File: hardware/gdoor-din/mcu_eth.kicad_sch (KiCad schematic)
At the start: 60 parts, among them J101 USB-C, J102 HR911105A, J103 EXP, SW101 RESET, SW102 BOOT, U101 ESP32-S3-WROOM-1-N8R2, U102 USBLC6-2SC6, U103 AMS1117-3.3, U104 W5500, Y101 25MHz

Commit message: gdoor-din: give SW101/SW102 one value so JLC merges their BOM line
Both buttons are the same part (C318884); the values RESET and BOOT
made two BOM lines matched to one part, which JLC flags. Both are now
"TL3342"; the schematic net labels still say which is which.

Co-Authored-By: Claude Opus 5.5 <noreply@anthropic.com>
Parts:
- SW101: value RESET -> TL3342
- SW102: value BOOT -> TL3342
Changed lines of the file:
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@@
 			)
 		)
-		(property "Value" "RESET"
+		(property "Value" "TL3342"
 			(at 99.06 80.01 0)
 			(show_name no)
@@
 			)
 		)
-		(property "Value" "BOOT"
+		(property "Value" "TL3342"
 			(at 99.06 92.71 0)
 			(show_name no)

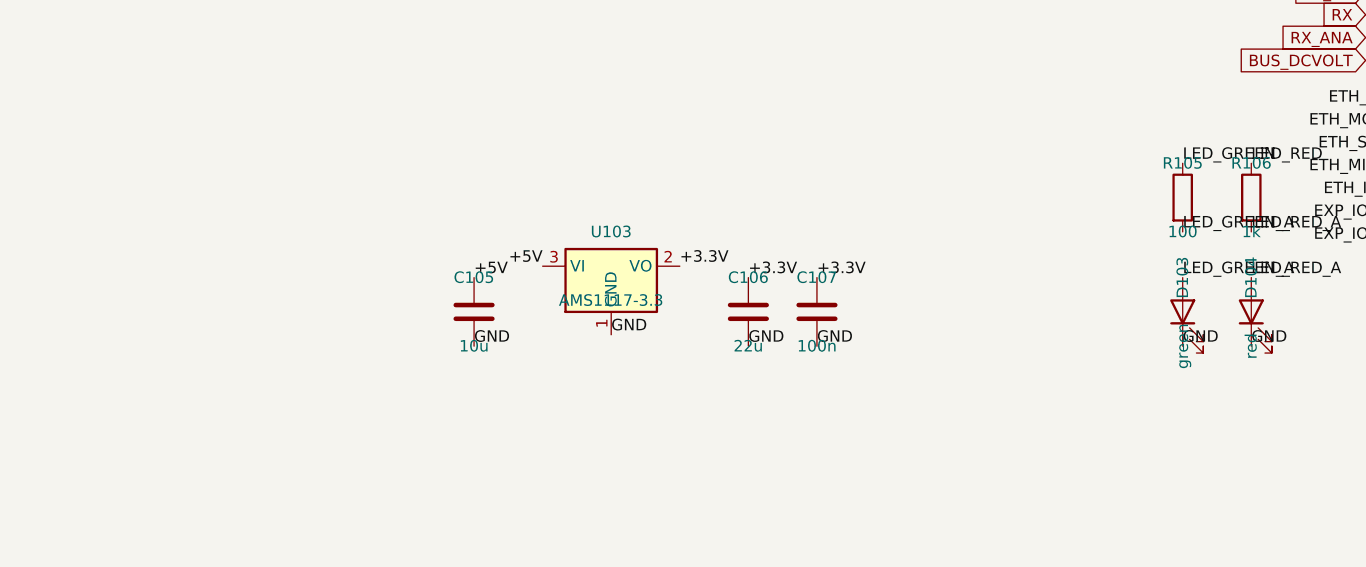
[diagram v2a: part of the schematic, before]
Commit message: gdoor-din: AP2114H regulator, front tab with flush RJ45 and USB-C
U103 (3.3 V digital) is now an AP2114H-3.3TRG1 (LCSC C150716): 1 A,
450 mV typ / 750 mV max dropout at 1 A, against about 1.1 V for the
AMS1117, so WiFi TX bursts do not brown out the S3. Same pinout as the
AMS1117 (1 GND, 2/tab VOUT, 3 VIN); the AP2114HA has a different one.
C104/C106 already meet the 4.7 uF minimum. JLC extended part.

The board gets a 6.8 x 40.4 mm front tab in the DIN window. J101 and
J102 move 8.45 mm forward (J102 also 0.8 mm down) with their Ethernet
and USB parts; their faces end 0.2 mm inside the window face. Tracks
crossing the moved block keep their shape and get connectors along the
move, so both halves of each pair grow equally (USB skew -4.20 mm, was
-4.17; Ethernet unchanged). 17 stitching vias under the moved parts are
gone. DRC: 0 errors, 0 unconnected, 0 parity issues.

Enclosure (first commit): 0.3 mm groove in the window wall for the tab,
body-sized RJ45 opening, tab in the fit-check ghost; fit check empty,
STLs rebuilt. JLC files and iBOMs regenerated (J101 CPL 97.09/-108.0).

Co-Authored-By: Claude Opus 5.5 <noreply@anthropic.com>
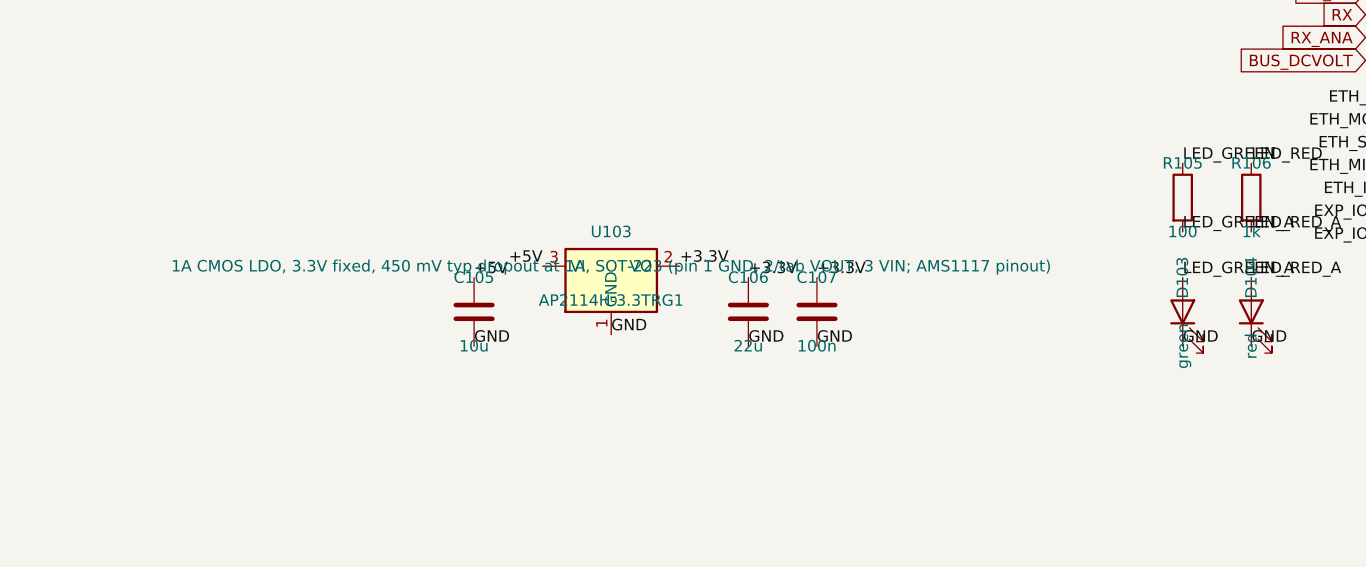
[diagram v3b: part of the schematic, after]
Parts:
- U103: value AMS1117-3.3 -> AP2114H-3.3TRG1; LCSC C6186 -> C150716
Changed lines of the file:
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@@
 			)
 		)
-		(property "Value" "AMS1117-3.3"
+		(property "Value" "AP2114H-3.3TRG1"
 			(at 50.8 130.81 0)
 			(show_name no)
@@
 			)
 		)
-		(property "Datasheet" ""
+		(property "Datasheet" "https://www.diodes.com/assets/Datasheets/AP2114.pdf"
 			(at 50.8 127 0)
 			(hide yes)
@@
 			)
 		)
-		(property "Description" ""
+		(property "Description" "1A CMOS LDO, 3.3V fixed, 450 mV typ dropout at 1A, SOT-223 (pin 1 GND, 2/tab VOUT, 3 VIN; AMS1117 pinout)"
 			(at 50.8 127 0)
 			(show_name no)
@@
 			)
 		)
-		(property "LCSC" "C6186"
+		(property "LCSC" "C150716"
 			(at 0 0 0)
 			(hide yes)
